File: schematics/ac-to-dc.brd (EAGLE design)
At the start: 23.8 x 21.6 mm, 12 parts, among them IC1 12V

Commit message: Trying to make sense of my head 3 years ago! :)
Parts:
- moved D2 3.81 mm to (5.08, 12.7)
- moved D3 3.81 mm to (5.08, 16.5)
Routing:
- net AGND: track 44.9 -> 0.00 mm
- net N$2: track 22.6 -> 0.00 mm
- net N$9: track 21.3 -> 0.00 mm
- net +12V: track 18.1 -> 0.00 mm
- net N$3: track 15.6 -> 0.00 mm
- net N$1: track 6.71 -> 0.00 mm
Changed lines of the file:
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@@
 <attribute name="NAME" x="16.51" y="20.32" size="0.4064" layer="25" ratio="12"/>
 </element>
-<element name="D2" library="gm-diodes" package="DO41-3" value="1N4001" x="5.08" y="16.51" smashed="yes" rot="R180">
-<attribute name="NAME" x="6.1722" y="17.145" size="1.27" layer="25" ratio="12" rot="R180"/>
-<attribute name="VALUE" x="0.635" y="14.224" size="0.4064" layer="27" ratio="12" rot="R180" align="top-right"/>
+<element name="D2" library="gm-diodes" package="DO41-3" value="1N4001" x="5.08" y="12.7" smashed="yes" rot="R180">
+<attribute name="NAME" x="6.1722" y="13.335" size="1.27" layer="25" ratio="12" rot="R180"/>
+<attribute name="VALUE" x="0.635" y="10.414" size="0.4064" layer="27" ratio="12" rot="R180" align="top-right"/>
 </element>
 <element name="C4" library="minimidi" package="E2,5-6" value="47uF/25V" x="13.97" y="10.16" smashed="yes" rot="R180">
@@
 <attribute name="VALUE" x="17.78" y="12.7" size="0.4064" layer="27" ratio="10" rot="R270"/>
 </element>
-<element name="D3" library="gm-diodes" package="DO41-3" value="1N4001" x="5.08" y="12.7" smashed="yes" rot="R180">
-<attribute name="NAME" x="6.1722" y="13.335" size="1.27" layer="25" ratio="12" rot="R180"/>
-<attribute name="VALUE" x="0.635" y="10.414" size="0.4064" layer="27" ratio="12" rot="R180" align="top-right"/>
+<element name="D3" library="gm-diodes" package="DO41-3" value="1N4001" x="5.08" y="16.51" smashed="yes" rot="R180">
+<attribute name="NAME" x="6.1722" y="17.145" size="1.27" layer="25" ratio="12" rot="R180"/>
+<attribute name="VALUE" x="0.635" y="14.224" size="0.4064" layer="27" ratio="12" rot="R180" align="top-right"/>
 </element>
 <element name="D4" library="gm-diodes" package="DO41-3" value="1N4001" x="5.08" y="8.89" smashed="yes">
@@
 <contactref element="D3" pad="C"/>
 <contactref element="XFRM" pad="2"/>
-<wire x1="1.3716" y1="20.1168" x2="8.6868" y2="12.8016" width="0.254" layer="1"/>
-<wire x1="8.6868" y1="12.8016" x2="8.89" y2="12.7" width="0.254" layer="1"/>
-<wire x1="1.3716" y1="20.1168" x2="1.27" y2="20.32" width="0.254" layer="1"/>
-<wire x1="5.2578" y1="9.144" x2="5.2578" y2="2.7432" width="0.254" layer="1"/>
-<wire x1="8.6868" y1="12.573" x2="5.2578" y2="9.144" width="0.254" layer="1"/>
-<wire x1="5.2578" y1="2.7432" x2="5.08" y2="2.54" width="0.254" layer="1"/>
-<wire x1="8.6868" y1="12.573" x2="8.89" y2="12.7" width="0.254" layer="1"/>
+<wire x1="1.27" y1="20.32" x2="8.89" y2="16.51" width="0" layer="19" extent="1-1"/>
+<wire x1="5.08" y1="2.54" x2="8.89" y2="16.51" width="0" layer="19" extent="1-1"/>
 </signal>
 <signal name="N$9">
@@
 <contactref element="D2" pad="C"/>
 <contactref element="C1" pad="+"/>
-<wire x1="8.9154" y1="20.3454" x2="12.573" y2="20.3454" width="0.254" layer="1"/>
-<wire x1="12.573" y1="20.3454" x2="12.7" y2="20.32" width="0.254" layer="1"/>
-<wire x1="8.9154" y1="20.3454" x2="8.89" y2="20.32" width="0.254" layer="1"/>
-<wire x1="8.9154" y1="20.1168" x2="8.9154" y2="16.6878" width="0.254" layer="1"/>
-<wire x1="8.9154" y1="16.6878" x2="8.89" y2="16.51" width="0.254" layer="1"/>
-<wire x1="8.9154" y1="20.1168" x2="8.89" y2="20.32" width="0.254" layer="1"/>
-<wire x1="8.9154" y1="7.3152" x2="8.9154" y2="3.8862" width="0.254" layer="1"/>
-<wire x1="10.0584" y1="8.4582" x2="8.9154" y2="7.3152" width="0.254" layer="1"/>
-<wire x1="10.0584" y1="15.3162" x2="10.0584" y2="8.4582" width="0.254" layer="1"/>
-<wire x1="8.9154" y1="16.4592" x2="10.0584" y2="15.3162" width="0.254" layer="1"/>
-<wire x1="8.9154" y1="3.8862" x2="8.89" y2="3.81" width="0.254" layer="1"/>
-<wire x1="8.9154" y1="16.4592" x2="8.89" y2="16.51" width="0.254" layer="1"/>
+<wire x1="8.89" y1="20.32" x2="12.7" y2="20.32" width="0" layer="19" extent="1-1"/>
+<wire x1="8.89" y1="12.7" x2="8.89" y2="20.32" width="0" layer="19" extent="1-1"/>
+<wire x1="8.89" y1="3.81" x2="8.89" y2="12.7" width="0" layer="19" extent="1-1"/>
 </signal>
 <signal name="+12V">
@@
 <contactref element="IC1" pad="OUT"/>
 <contactref element="PWR" pad="1"/>
-<wire x1="16.4592" y1="11.43" x2="20.32" y2="11.43" width="0.254" layer="1"/>
-<wire x1="15.3162" y1="10.287" x2="16.4592" y2="11.43" width="0.254" layer="1"/>
-<wire x1="15.3162" y1="10.287" x2="15.24" y2="10.16" width="0.254" layer="1"/>
-<wire x1="15.3162" y1="12.573" x2="15.3162" y2="16.4592" width="0.254" layer="1"/>
-<wire x1="16.4592" y1="11.43" x2="15.3162" y2="12.573" width="0.254" layer="1"/>
-<wire x1="15.3162" y1="16.4592" x2="15.24" y2="16.51" width="0.254" layer="1"/>
-<wire x1="21.4884" y1="10.287" x2="21.4884" y2="5.2578" width="0.254" layer="1"/>
-<wire x1="20.3454" y1="11.43" x2="21.4884" y2="10.287" width="0.254" layer="1"/>
-<wire x1="21.4884" y1="5.2578" x2="21.59" y2="5.08" width="0.254" layer="1"/>
-<wire x1="20.3454" y1="11.43" x2="20.32" y2="11.43" width="0.254" layer="1"/>
+<wire x1="15.24" y1="10.16" x2="15.24" y2="16.51" width="0" layer="19" extent="1-1"/>
+<wire x1="20.32" y1="11.43" x2="15.24" y2="10.16" width="0" layer="19" extent="1-1"/>
+<wire x1="21.59" y1="5.08" x2="20.32" y2="11.43" width="0" layer="19" extent="1-1"/>
 </signal>
 <signal name="AGND">
@@
 <contactref element="IC1" pad="GND"/>
 <contactref element="PWR" pad="2"/>
-<wire x1="15.0876" y1="14.1732" x2="20.1168" y2="14.1732" width="0.254" layer="16"/>
-<wire x1="12.8016" y1="16.4592" x2="15.0876" y2="14.1732" width="0.254" layer="16"/>
-<wire x1="20.1168" y1="14.1732" x2="20.32" y2="13.97" width="0.254" layer="16"/>
-<wire x1="12.8016" y1="16.4592" x2="12.7" y2="16.51" width="0.254" layer="16"/>
-<wire x1="5.0292" y1="12.573" x2="1.3716" y2="12.573" width="0.254" layer="16"/>
-<wire x1="8.6868" y1="8.9154" x2="5.0292" y2="12.573" width="0.254" layer="16"/>
-<wire x1="1.3716" y1="12.573" x2="1.27" y2="12.7" width="0.254" layer="16"/>
-<wire x1="8.6868" y1="8.9154" x2="8.89" y2="8.89" width="0.254" layer="16"/>
-<wire x1="11.43" y1="6.1722" x2="11.43" y2="3.81" width="0.254" layer="16"/>
-<wire x1="8.9154" y1="8.6868" x2="10.0584" y2="7.5438" width="0.254" layer="16"/>
-<wire x1="10.0584" y1="7.5438" x2="11.43" y2="6.1722" width="0.254" layer="16"/>
-<wire x1="8.9154" y1="8.6868" x2="8.89" y2="8.89" width="0.254" layer="16"/>
-<wire x1="10.0584" y1="7.5438" x2="12.573" y2="10.0584" width="0.254" layer="16"/>
-<wire x1="12.573" y1="10.0584" x2="12.7" y2="10.16" width="0.254" layer="16"/>
-<wire x1="18.9738" y1="5.2578" x2="21.4884" y2="2.7432" width="0.254" layer="16"/>
-<wire x1="18.9738" y1="5.4864" x2="18.9738" y2="5.2578" width="0.254" layer="16"/>
-<wire x1="17.8308" y1="6.6294" x2="18.9738" y2="5.4864" width="0.254" layer="16"/>
-<wire x1="11.8872" y1="6.6294" x2="17.8308" y2="6.6294" width="0.254" layer="16"/>
-<wire x1="11.43" y1="6.1722" x2="11.8872" y2="6.6294" width="0.254" layer="16"/>
-<wire x1="21.4884" y1="2.7432" x2="21.59" y2="2.54" width="0.254" layer="16"/>
-<wire x1="15.0876" y1="12.573" x2="15.0876" y2="14.1732" width="0.254" layer="16"/>
-<wire x1="12.8016" y1="10.287" x2="15.0876" y2="12.573" width="0.254" layer="16"/>
-<wire x1="12.8016" y1="10.287" x2="12.7" y2="10.16" width="0.254" layer="16"/>
+<wire x1="12.7" y1="16.51" x2="20.32" y2="13.97" width="0" layer="19" extent="1-1"/>
+<wire x1="12.7" y1="10.16" x2="12.7" y2="16.51" width="0" layer="19" extent="1-1"/>
+<wire x1="8.89" y1="8.89" x2="12.7" y2="10.16" width="0" layer="19" extent="1-1"/>
+<wire x1="11.43" y1="3.81" x2="8.89" y2="8.89" width="0" layer="19" extent="1-1"/>
+<wire x1="21.59" y1="2.54" x2="11.43" y2="3.81" width="0" layer="19" extent="1-1"/>
+<wire x1="1.27" y1="16.51" x2="8.89" y2="8.89" width="0" layer="19" extent="1-1"/>
 </signal>
 <signal name="N$3">
@@
 <contactref element="D2" pad="A"/>
 <contactref element="XFRM" pad="1"/>
-<wire x1="1.3716" y1="3.8862" x2="1.3716" y2="8.6868" width="0.254" layer="1"/>
-<wire x1="2.5146" y1="2.7432" x2="1.3716" y2="3.8862" width="0.254" layer="1"/>
-<wire x1="1.3716" y1="8.6868" x2="1.27" y2="8.89" width="0.254" layer="1"/>
-<wire x1="2.5146" y1="2.7432" x2="2.54" y2="2.54" width="0.254" layer="1"/>
-<wire x1="1.3716" y1="14.1732" x2="1.3716" y2="16.4592" width="0.254" layer="1"/>
-<wire x1="2.5146" y1="13.0302" x2="1.3716" y2="14.1732" width="0.254" layer="1"/>
-<wire x1="2.5146" y1="10.0584" x2="2.5146" y2="13.0302" width="0.254" layer="1"/>
-<wire x1="1.3716" y1="8.9154" x2="2.5146" y2="10.0584" width="0.254" layer="1"/>
-<wire x1="1.3716" y1="16.4592" x2="1.27" y2="16.51" width="0.254" layer="1"/>
-<wire x1="1.3716" y1="8.9154" x2="1.27" y2="8.89" width="0.254" layer="1"/>
+<wire x1="1.27" y1="8.89" x2="1.27" y2="12.7" width="0" layer="19" extent="1-1"/>
+<wire x1="2.54" y1="2.54" x2="1.27" y2="8.89" width="0" layer="19" extent="1-1"/>
 </signal>
 <signal name="N$1">
 <contactref element="IC1" pad="IN"/>
 <contactref element="TOGGLE" pad="2"/>
-<wire x1="16.6878" y1="20.1168" x2="15.3162" y2="20.1168" width="0.254" layer="1"/>
-<wire x1="20.1168" y1="16.6878" x2="16.6878" y2="20.1168" width="0.254" layer="1"/>
-<wire x1="15.3162" y1="20.1168" x2="15.24" y2="20.32" width="0.254" layer="1"/>
-<wire x1="20.1168" y1="16.6878" x2="20.32" y2="16.51" width="0.254" layer="1"/>
+<wire x1="15.24" y1="20.32" x2="20.32" y2="16.51" width="0" layer="19" extent="1-1"/>
 </signal>
 </signals>

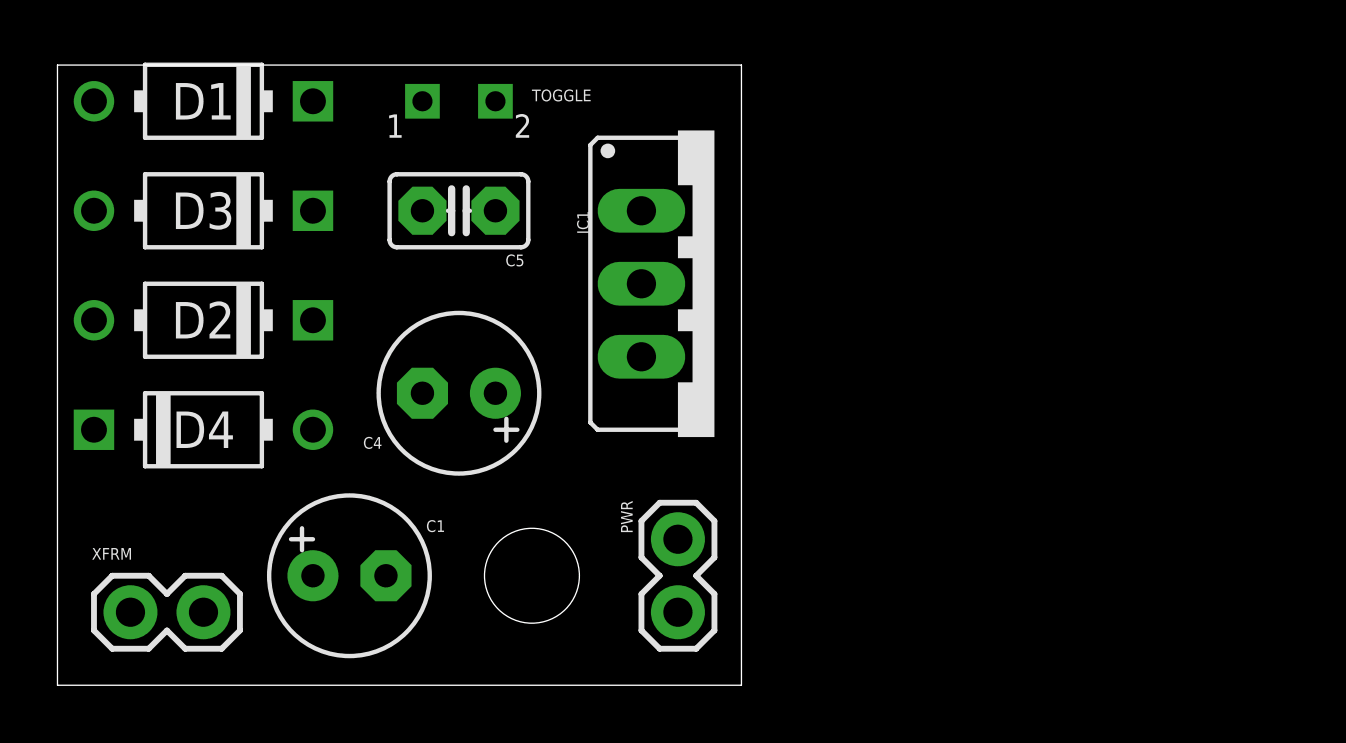
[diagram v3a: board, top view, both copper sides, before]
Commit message: Added an LED to the ac-to-dc board
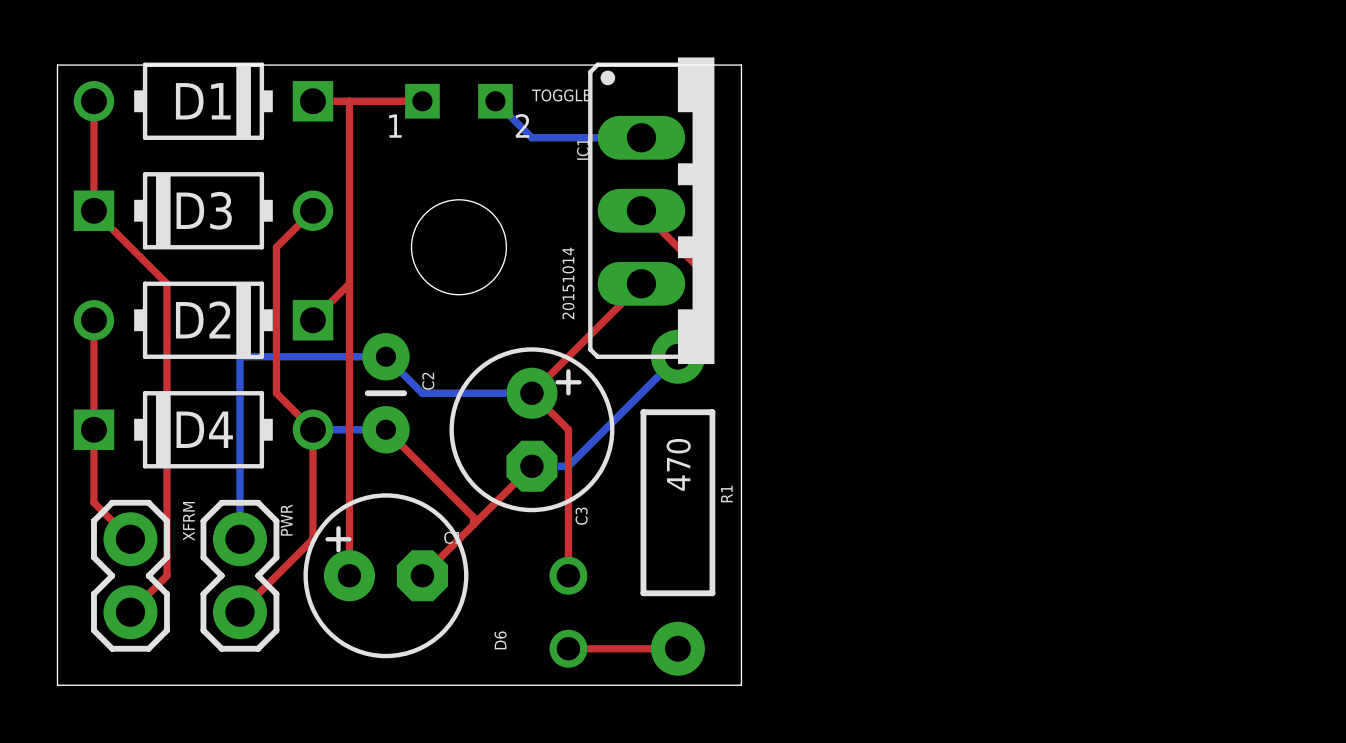
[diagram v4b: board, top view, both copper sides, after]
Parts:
- removed C4: 47uF/25V, minimidi:E2,5-6
- removed C5: 0.1uF, minimidi:C025-025X050
- added C2: 0.1uF, SparkFun-Capacitors:CAP-PTH-SMALL
- added C3: 47uF/25V, minimidi:E2,5-6
- added D6: (no value), SparkFun-LED:LED3MM-NS
- added R1: 470, SparkFun-Resistors:AXIAL-0.4
- D1, D2, D3, D4: value 1N4001 -> 1N4007
- moved PWR 15.2 mm to (6.35, 5.08)
- moved JP1 11.7 mm to (14.0, 15.2)
- moved IC1 2.54 mm to (22.9, 16.5)
- moved XFRM 2.54 mm to (2.54, 5.08), turned to 270 degrees
- moved C1 1.27 mm to (11.4, 3.81)
- turned D3 to 0 degrees
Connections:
- new net N$4: D6.K, R1.P$2
- net +12V: now also C2.1, C3.+, D6.A; no longer C4.+, C5.1
- net AGND: now also C2.2, C3.-, R1.P$1; no longer C4.-, C5.2
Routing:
- net AGND: track 0.00 -> 41.5 mm
- net +12V: track 0.00 -> 29.3 mm
- net N$9: track 0.00 -> 22.1 mm
- net N$2: track 0.00 -> 19.4 mm
- net N$3: track 0.00 -> 8.15 mm
- net N$1: track 0.00 -> 5.61 mm
- net N$4: track 0.00 -> 3.81 mm
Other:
- board text added: "20151014"
